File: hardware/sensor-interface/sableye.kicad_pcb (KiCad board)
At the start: 2 copper layers, 9 parts, among them J1 Conn_PiWR-Pi2C-PiLERTs, J2 Conn_A0x48-9, J3 Conn_A0x4A-B, J4 Conn_Bonus-I2C, U1 ADS1115, U2 ADS1115, U3 ADS1115, U4 ADS1115

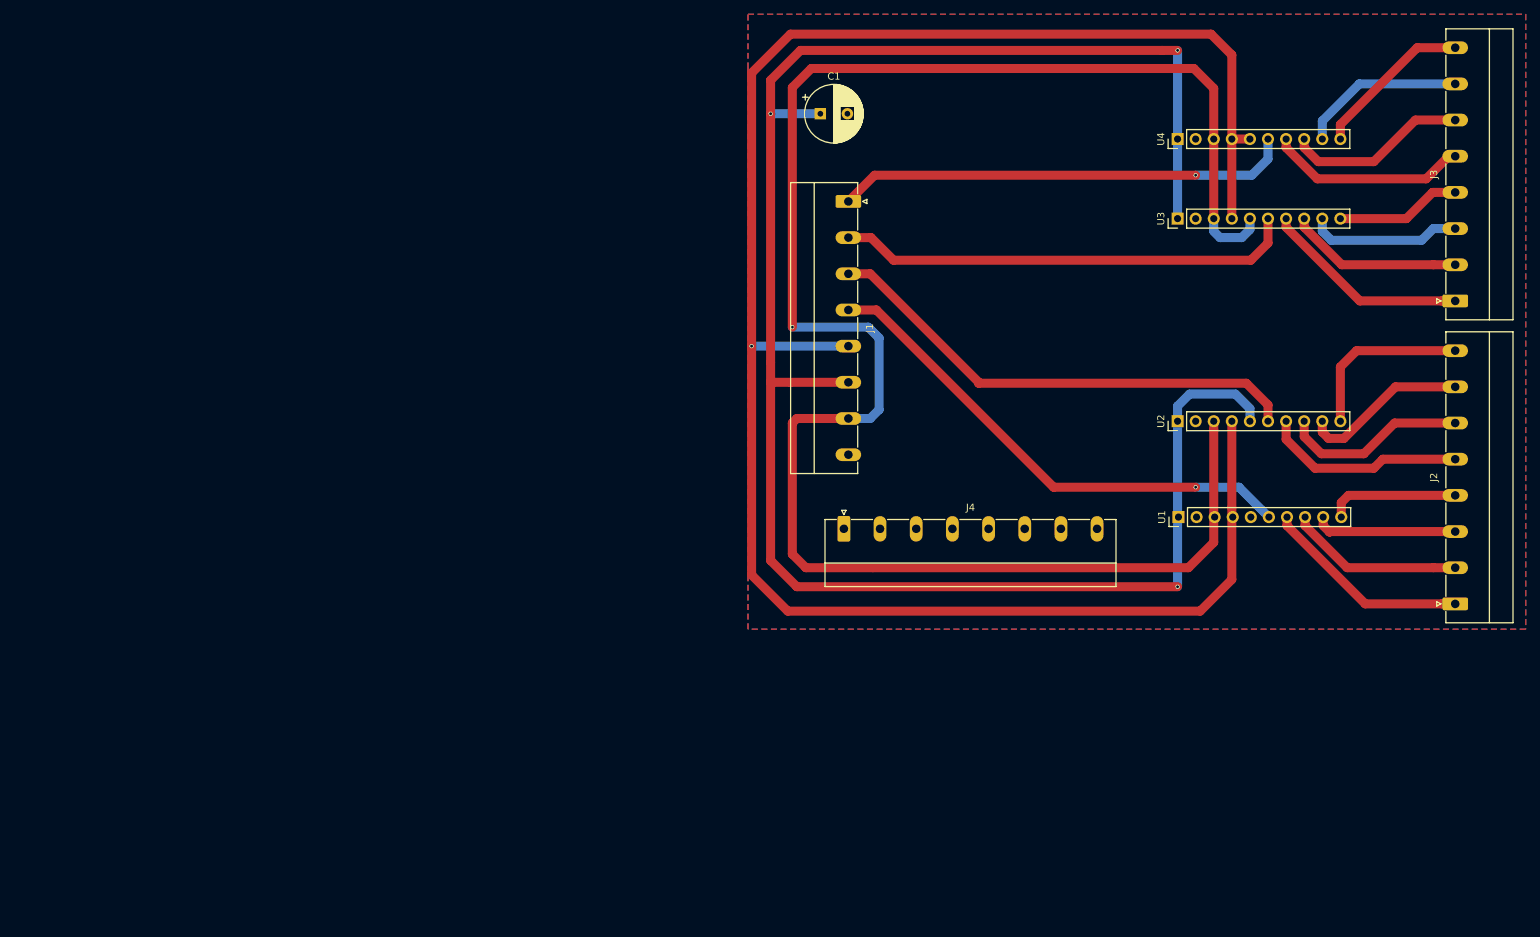
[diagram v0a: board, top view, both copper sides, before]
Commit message: Started re-re-design i2c interface board for fitting more ADCs onboard; needs some more work to accommodate other sensors
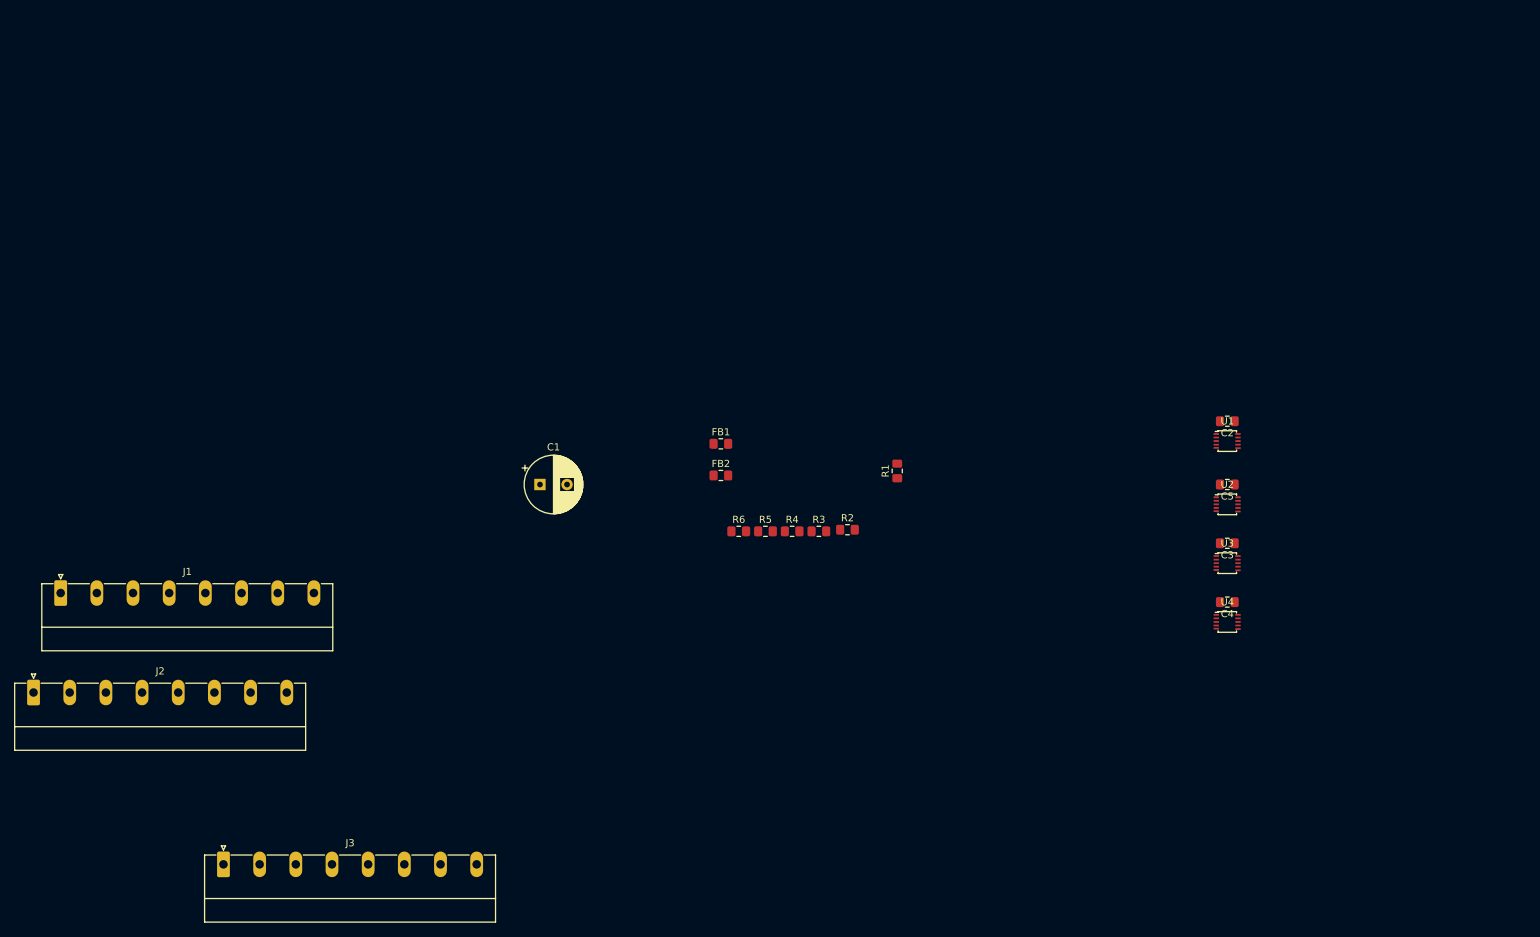
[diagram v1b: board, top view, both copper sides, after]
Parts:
- removed J4: Conn_Bonus-I2C, Connector_Phoenix_MC_HighVoltage:PhoenixContact_MC_1,5_8-G-5.08_1x08_P5.08mm_Horizontal
- added C2: 1uF, Capacitor_SMD:C_0805_2012Metric_Pad1.15x1.40mm_HandSolder, F.Cu at (185.4, 87.6)
- added C3: 1uF, Capacitor_SMD:C_0805_2012Metric_Pad1.15x1.40mm_HandSolder, F.Cu at (185.4, 104.8)
- added C4: 1uF, Capacitor_SMD:C_0805_2012Metric_Pad1.15x1.40mm_HandSolder, F.Cu at (185.4, 113.0)
- added C5: 1uF, Capacitor_SMD:C_0805_2012Metric_Pad1.15x1.40mm_HandSolder, F.Cu at (185.4, 96.5)
- added FB1: MMZ2012Y152B, Inductor_SMD:L_0805_2012Metric_Pad1.15x1.40mm_HandSolder, F.Cu at (114.3, 90.8)
- added FB2: MMZ2012Y152B, Inductor_SMD:L_0805_2012Metric_Pad1.15x1.40mm_HandSolder, F.Cu at (114.3, 95.2)
- added R1: 10k, Resistor_SMD:R_0805_2012Metric_Pad1.15x1.40mm_HandSolder, F.Cu at (139.1, 94.6)
- added R2: 10k, Resistor_SMD:R_0805_2012Metric_Pad1.15x1.40mm_HandSolder, F.Cu at (132.1, 102.9)
- added R3: 10k, Resistor_SMD:R_0805_2012Metric_Pad1.15x1.40mm_HandSolder, F.Cu at (128.1, 103.1)
- added R4: 10k, Resistor_SMD:R_0805_2012Metric_Pad1.15x1.40mm_HandSolder, F.Cu at (124.3, 103.1)
- added R5: 10k, Resistor_SMD:R_0805_2012Metric_Pad1.15x1.40mm_HandSolder, F.Cu at (120.6, 103.1)
- added R6: 10k, Resistor_SMD:R_0805_2012Metric_Pad1.15x1.40mm_HandSolder, F.Cu at (116.8, 103.1)
- C1: value C_PWR (optional) -> 1uF
- U1, U2, U3, U4: footprint Connector_PinHeader_2.54mm:PinHeader_1x10_P2.54mm_Vertical -> Radishes:VSSOP-10_2.4x2.1mm_P0.5mm
- moved J2 200.0 mm to (17.8, 125.7), turned to 0 degrees
- moved J3 190.2 mm to (44.5, 149.9), turned to 0 degrees
- moved J1 123.5 mm to (21.6, 111.8), turned to 0 degrees
- moved U4 67.9 mm to (185.4, 115.6), turned to 0 degrees
- moved C1 65.3 mm to (88.9, 96.5)
- moved U3 48.6 mm to (185.4, 107.3), turned to 0 degrees
- moved U2 13.4 mm to (185.4, 99.1), turned to 0 degrees
- moved U1 12.9 mm to (185.4, 90.2), turned to 0 degrees
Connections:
- C1 pad 1: VDD -> Net-(C1-Pad1)
- C1 pad 2: GND -> Net-(C1-Pad2)
- J1 pad 6: VDD -> Net-(C1-Pad2)
- J1 pad 8: GND -> Net-(C1-Pad1)
- U1 pad 1: VDD -> GND
- U1 pad 10: Net-(J2-Pad4) -> SCLK
- U1 pad 2: GND -> ALERT_0x48
- U1 pad 3: SCLK -> GND
- U1 pad 4: SDA -> Net-(J2-Pad1)
- U1 pad 5: GND -> Net-(J2-Pad2)
- U1 pad 6: ALERT_0x48 -> Net-(J2-Pad3)
- U1 pad 7: Net-(J2-Pad1) -> Net-(J2-Pad4)
- U1 pad 8: Net-(J2-Pad2) -> VDD
- U1 pad 9: Net-(J2-Pad3) -> SDA
- U2 pad 10: Net-(J2-Pad8) -> SCLK
- U2 pad 2: GND -> ALERT_0x49
- U2 pad 3: SCLK -> GND
- U2 pad 4: SDA -> Net-(J2-Pad5)
- U2 pad 5: VDD -> Net-(J2-Pad6)
- U2 pad 6: ALERT_0x49 -> Net-(J2-Pad7)
- U2 pad 7: Net-(J2-Pad5) -> Net-(J2-Pad8)
- U2 pad 8: Net-(J2-Pad6) -> VDD
- U2 pad 9: Net-(J2-Pad7) -> SDA
- U3 pad 1: VDD -> SCLK
- U3 pad 10: Net-(J3-Pad4) -> SCLK
- U3 pad 2: GND -> ALERT_0x4A
- U3 pad 3: SCLK -> GND
- U3 pad 4: SDA -> Net-(J3-Pad1)
- U3 pad 5: SCLK -> Net-(J3-Pad2)
- U3 pad 6: ALERT_0x4A -> Net-(J3-Pad3)
- U3 pad 7: Net-(J3-Pad1) -> Net-(J3-Pad4)
- U3 pad 8: Net-(J3-Pad2) -> VDD
- U3 pad 9: Net-(J3-Pad3) -> SDA
- U4 pad 1: VDD -> SDA
- U4 pad 10: Net-(J3-Pad8) -> SCLK
- U4 pad 2: GND -> ALERT_0x4B
- U4 pad 3: SCLK -> GND
- U4 pad 4: SDA -> Net-(J3-Pad5)
- U4 pad 5: SDA -> Net-(J3-Pad6)
- U4 pad 6: ALERT_0x4B -> Net-(J3-Pad7)
- U4 pad 7: Net-(J3-Pad5) -> Net-(J3-Pad8)
- U4 pad 8: Net-(J3-Pad6) -> VDD
- U4 pad 9: Net-(J3-Pad7) -> SDA
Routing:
- net SDA: track 274.1 -> 0.00 mm, vias 1 -> 0
- net VDD: track 265.4 -> 0.00 mm, vias 3 -> 0
- net SCLK: track 255.3 -> 0.00 mm, vias 1 -> 0
- net ALERT_0x48: track 71.1 -> 0.00 mm, vias 1 -> 0
- net ALERT_0x49: track 68.9 -> 0.00 mm
- net ALERT_0x4A: track 64.7 -> 0.00 mm
- net ALERT_0x4B: track 64.2 -> 0.00 mm, vias 1 -> 0
- net Net-(J2-Pad1): track 29.4 -> 0.00 mm
- net Net-(J3-Pad1): track 29.2 -> 0.00 mm
- net Net-(J3-Pad5): track 29.0 -> 0.00 mm
- net Net-(J2-Pad5): track 28.5 -> 0.00 mm
- net Net-(J3-Pad6): track 26.5 -> 0.00 mm
- net Net-(J2-Pad6): track 26.2 -> 0.00 mm
- net Net-(J2-Pad2): track 24.7 -> 0.00 mm
- net Net-(J2-Pad8): track 24.7 -> 0.00 mm
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- removed copper zone on B.Cu, net GND
- removed copper zone on F.Cu, net GND
